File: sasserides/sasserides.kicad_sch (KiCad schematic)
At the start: 128 parts, among them J1 Conn_02x16_Odd_Even, Q1 2N7002

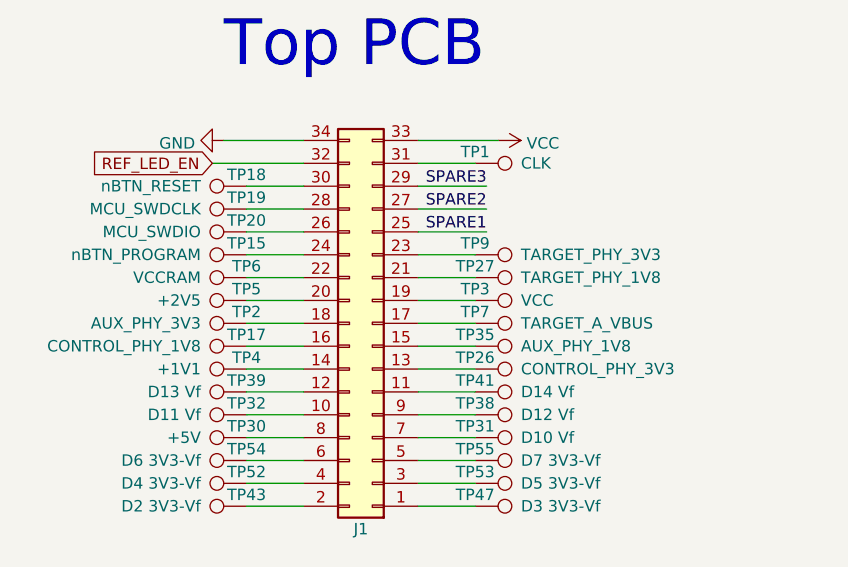
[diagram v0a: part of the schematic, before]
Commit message: Fix test points
	*Move TP7, TP9, & TP15 to correct locations
	*Swap TARGET_A_VBUS AND AUX_PHY_3V3 on MUX1
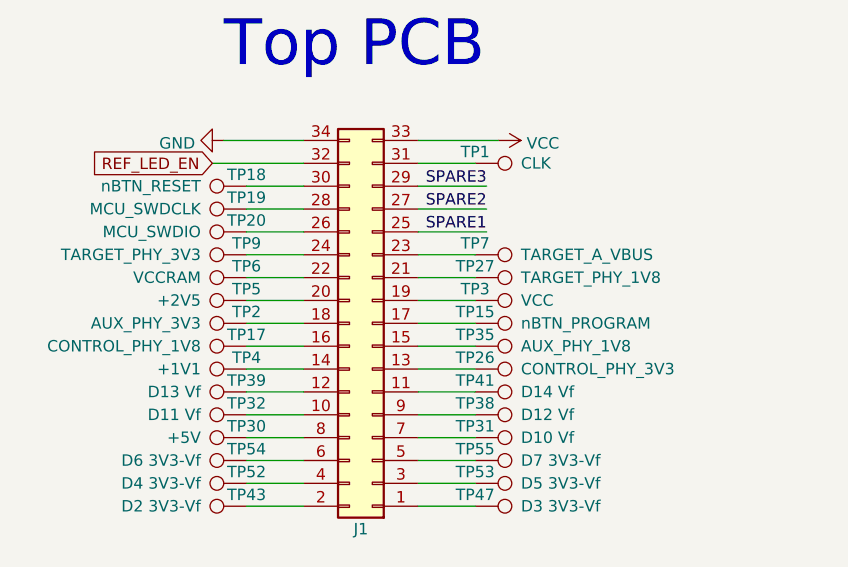
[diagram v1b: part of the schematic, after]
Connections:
- net at J1.17 (Pin_17): now also TP15.1; no longer TP7.1
- net at J1.23 (Pin_23): now also TP7.1; no longer TP9.1
- net at J1.24 (Pin_24): now also TP9.1; no longer TP15.1
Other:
- moved on the sheet: TP15, TP7, TP9
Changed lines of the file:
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@@
     )
   )
-  (symbol (lib_id "Connector:TestPoint") (at 91.44 72.39 270) (mirror x) (unit 1)
+  (symbol (lib_id "Connector:TestPoint") (at 91.44 64.77 270) (mirror x) (unit 1)
     (in_bom yes) (on_board yes) (dnp no)
-    (property "Reference" "TP7" (at 91.44 71.12 90)
+    (property "Reference" "TP7" (at 91.44 63.5 90)
       (effects (font (size 1.27 1.27)))
     )
-    (property "Value" "TARGET_A_VBUS" (at 96.52 72.39 90)
+    (property "Value" "TARGET_A_VBUS" (at 96.52 64.77 90)
       (effects (font (size 1.27 1.27)) (justify left))
     )
-    (property "Footprint" "tycho:HEADER-1x1-TESTPROBE" (at 91.44 67.31 0)
+    (property "Footprint" "tycho:HEADER-1x1-TESTPROBE" (at 91.44 59.69 0)
       (effects (font (size 1.27 1.27)) hide)
     )
-    (property "Datasheet" "~" (at 91.44 67.31 0)
+    (property "Datasheet" "~" (at 91.44 59.69 0)
       (effects (font (size 1.27 1.27)) hide)
     )
-    (property "Manufacturer" "Harwin Inc." (at 91.44 72.39 0)
+    (property "Manufacturer" "Harwin Inc." (at 91.44 64.77 0)
       (effects (font (size 1.27 1.27)) hide)
     )
-    (property "Part Number" "S25-512" (at 91.44 72.39 0)
+    (property "Part Number" "S25-512" (at 91.44 64.77 0)
       (effects (font (size 1.27 1.27)) hide)
     )
-    (property "Description" "SPRING PROBE SLEEVE" (at 91.44 72.39 0)
+    (property "Description" "SPRING PROBE SLEEVE" (at 91.44 64.77 0)
       (effects (font (size 1.27 1.27)) hide)
     )
@@
     )
   )
-  (symbol (lib_id "Connector:TestPoint") (at 91.44 64.77 270) (mirror x) (unit 1)
+  (symbol (lib_id "Connector:TestPoint") (at 66.04 64.77 90) (mirror x) (unit 1)
     (in_bom yes) (on_board yes) (dnp no)
-    (property "Reference" "TP9" (at 91.44 63.5 90)
+    (property "Reference" "TP9" (at 66.04 63.5 90)
       (effects (font (size 1.27 1.27)))
     )
-    (property "Value" "TARGET_PHY_3V3" (at 96.52 64.77 90)
+    (property "Value" "TARGET_PHY_3V3" (at 60.96 64.77 90)
       (effects (font (size 1.27 1.27)) (justify left))
     )
-    (property "Footprint" "tycho:HEADER-1x1-TESTPROBE" (at 91.44 59.69 0)
+    (property "Footprint" "tycho:HEADER-1x1-TESTPROBE" (at 66.04 69.85 0)
       (effects (font (size 1.27 1.27)) hide)
     )
-    (property "Datasheet" "~" (at 91.44 59.69 0)
+    (property "Datasheet" "~" (at 66.04 69.85 0)
       (effects (font (size 1.27 1.27)) hide)
     )
-    (property "Manufacturer" "Harwin Inc." (at 91.44 64.77 0)
+    (property "Manufacturer" "Harwin Inc." (at 66.04 64.77 0)
       (effects (font (size 1.27 1.27)) hide)
     )
-    (property "Part Number" "S25-512" (at 91.44 64.77 0)
+    (property "Part Number" "S25-512" (at 66.04 64.77 0)
       (effects (font (size 1.27 1.27)) hide)
     )
-    (property "Description" "SPRING PROBE SLEEVE" (at 91.44 64.77 0)
+    (property "Description" "SPRING PROBE SLEEVE" (at 66.04 64.77 0)
       (effects (font (size 1.27 1.27)) hide)
     )
@@
     )
   )
-  (symbol (lib_id "Connector:TestPoint") (at 66.04 64.77 90) (unit 1)
+  (symbol (lib_id "Connector:TestPoint") (at 91.44 72.39 270) (unit 1)
     (in_bom yes) (on_board yes) (dnp no)
-    (property "Reference" "TP15" (at 66.04 63.5 90)
+    (property "Reference" "TP15" (at 91.44 71.12 90)
       (effects (font (size 1.27 1.27)))
     )
-    (property "Value" "nBTN_PROGRAM" (at 60.96 64.77 90)
+    (property "Value" "nBTN_PROGRAM" (at 96.52 72.39 90)
       (effects (font (size 1.27 1.27)) (justify left))
     )
-    (property "Footprint" "tycho:HEADER-1x1-TESTPROBE" (at 66.04 59.69 0)
+    (property "Footprint" "tycho:HEADER-1x1-TESTPROBE" (at 91.44 77.47 0)
       (effects (font (size 1.27 1.27)) hide)
     )
-    (property "Datasheet" "~" (at 66.04 59.69 0)
+    (property "Datasheet" "~" (at 91.44 77.47 0)
       (effects (font (size 1.27 1.27)) hide)
     )
-    (property "Manufacturer" "Harwin Inc." (at 66.04 64.77 0)
+    (property "Manufacturer" "Harwin Inc." (at 91.44 72.39 0)
       (effects (font (size 1.27 1.27)) hide)
     )
-    (property "Part Number" "S25-512" (at 66.04 64.77 0)
+    (property "Part Number" "S25-512" (at 91.44 72.39 0)
       (effects (font (size 1.27 1.27)) hide)
     )
-    (property "Description" "SPRING PROBE SLEEVE" (at 66.04 64.77 0)
+    (property "Description" "SPRING PROBE SLEEVE" (at 91.44 72.39 0)
       (effects (font (size 1.27 1.27)) hide)
     )

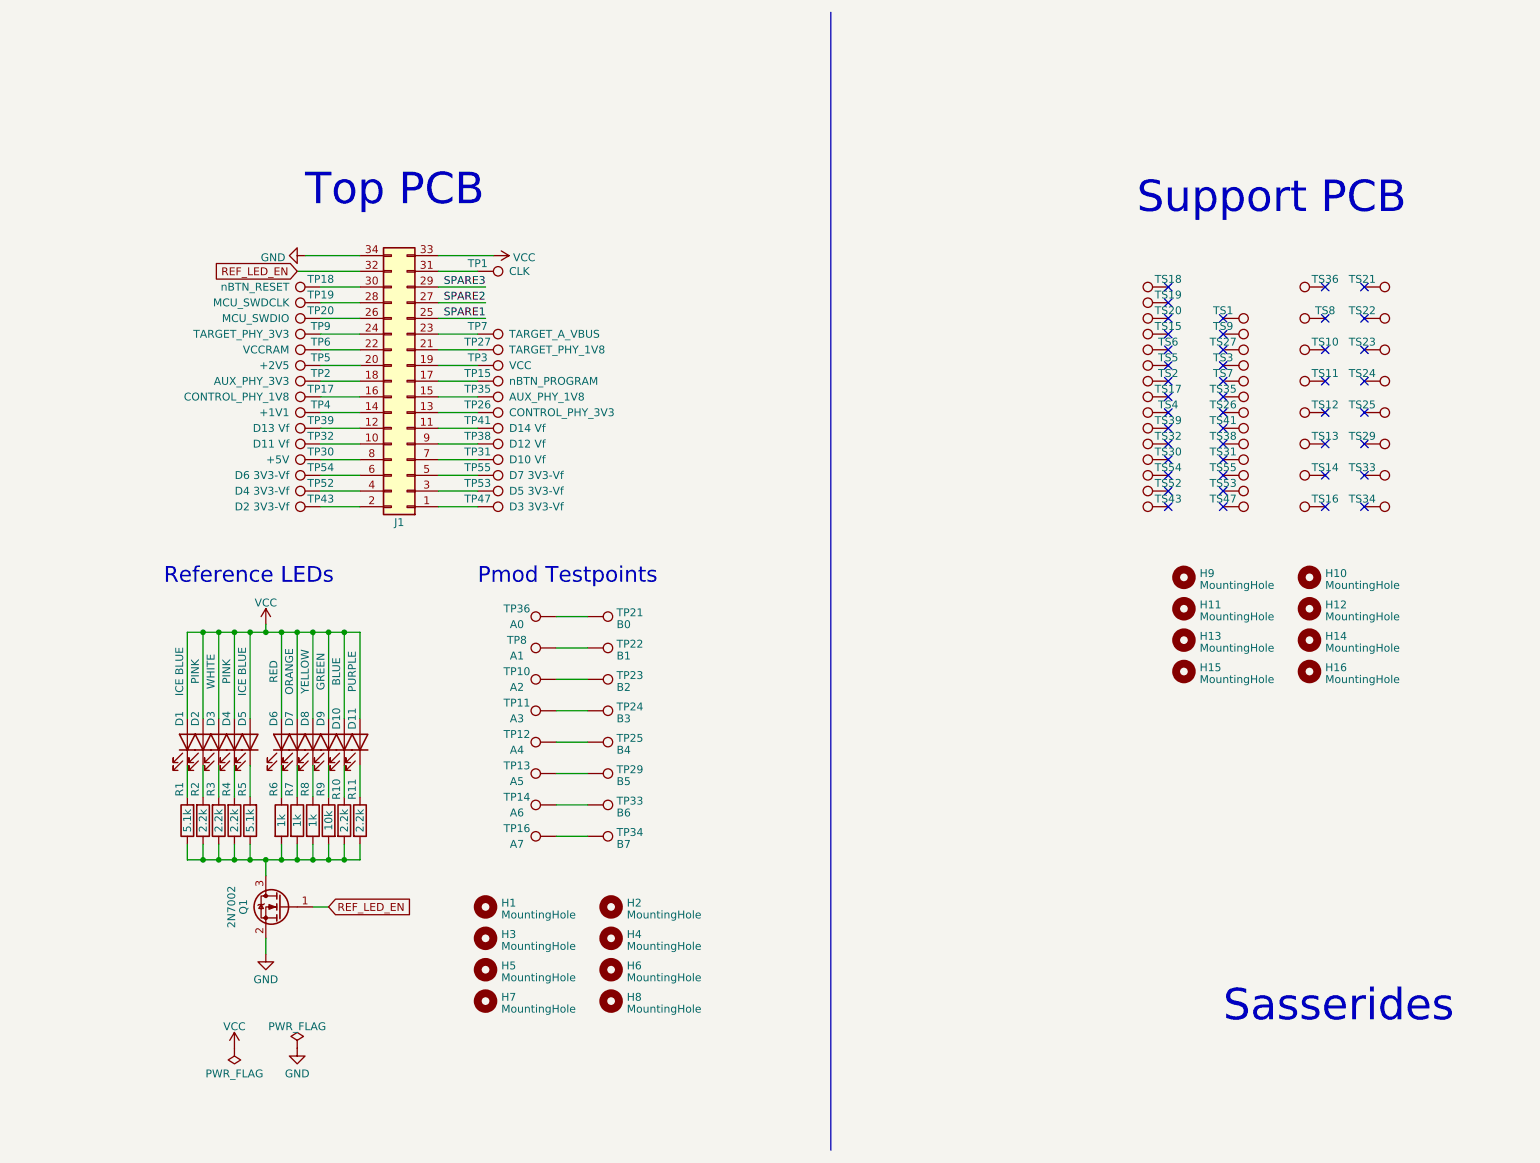
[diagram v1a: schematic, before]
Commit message: Rename Pmod TPs to A0-7/B0-7
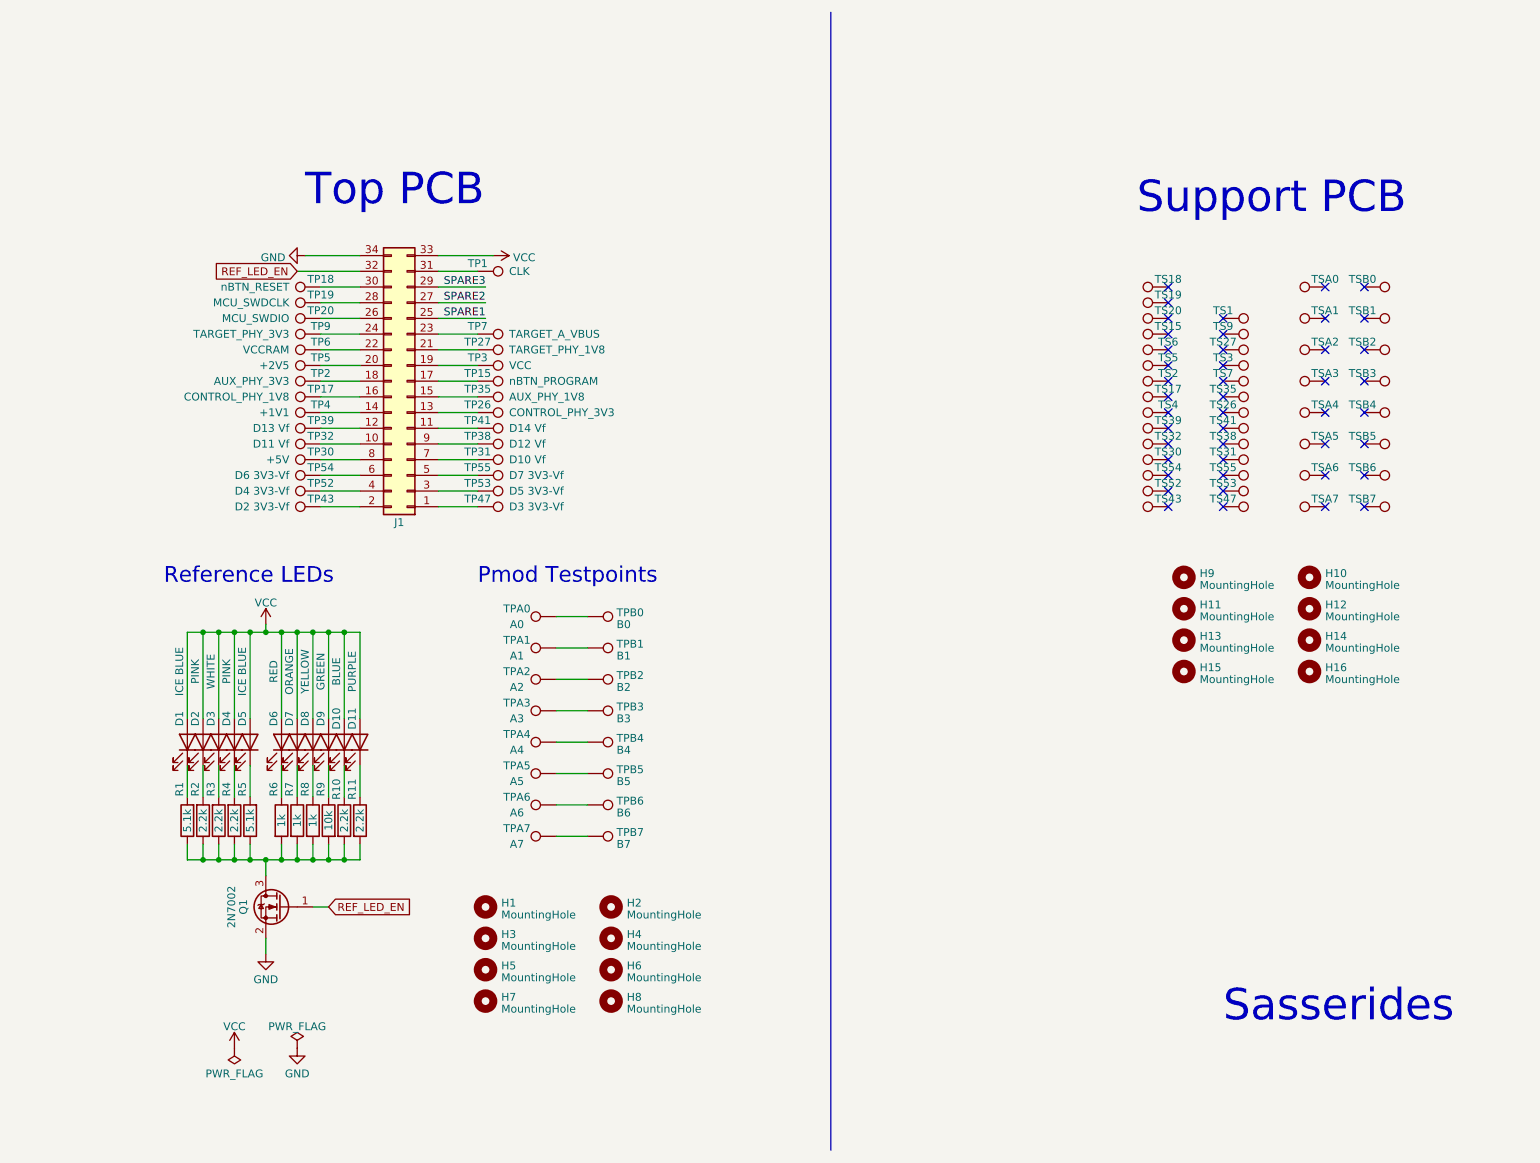
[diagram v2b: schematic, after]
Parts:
- renumbered TP36 to TPA0, TP8 to TPA1, TP10 to TPA2, TP11 to TPA3, TP12 to TPA4, TP13 to TPA5, TP14 to TPA6, TP16 to TPA7, TP21 to TPB0, TP22 to TPB1, TP23 to TPB2, TP24 to TPB3, TP25 to TPB4, TP29 to TPB5, TP33 to TPB6, TP34 to TPB7, TS36 to TSA0, TS8 to TSA1, TS10 to TSA2, TS11 to TSA3, TS12 to TSA4, TS13 to TSA5, TS14 to TSA6, TS16 to TSA7, TS21 to TSB0, TS22 to TSB1, TS23 to TSB2, TS24 to TSB3, TS25 to TSB4, TS29 to TSB5, TS33 to TSB6, TS34 to TSB7

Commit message: Clean up Sasserides silkscreen; Add meta data to all sheets
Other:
- company: (none) -> Copyright 2023 Great Scott Gadgets
- title: (none) -> Sasserides
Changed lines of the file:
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@@
 (kicad_sch (version 20230121) (generator eeschema)
   (paper "A4")
+  (title_block
+    (title "Sasserides")
+    (date "${DATE}")
+    (rev "${VERSION}")
+    (company "Copyright 2023 Great Scott Gadgets")
+    (comment 1 "Licensed under the CERN-OHL-P v2")
+  )
   (junction (at 49.53 113.03) (diameter 0) (color 0 0 0 0)
   )

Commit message: Change 34 pin header on Sasserides-A to shrouded type.
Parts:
- J1: footprint Connector_PinHeader_2.54mm:PinHeader_2x17_P2.54mm_Vertical -> tycho:shrouded_pin-header_2x17
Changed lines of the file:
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@@
       (effects (font (size 1.27 1.27)) hide)
     )
-    (property "Footprint" "Connector_PinHeader_2.54mm:PinHeader_2x17_P2.54mm_Vertical" (at 80.01 72.39 0)
+    (property "Footprint" "tycho:shrouded_pin-header_2x17" (at 80.01 72.39 0)
       (effects (font (size 1.27 1.27)) hide)
     )

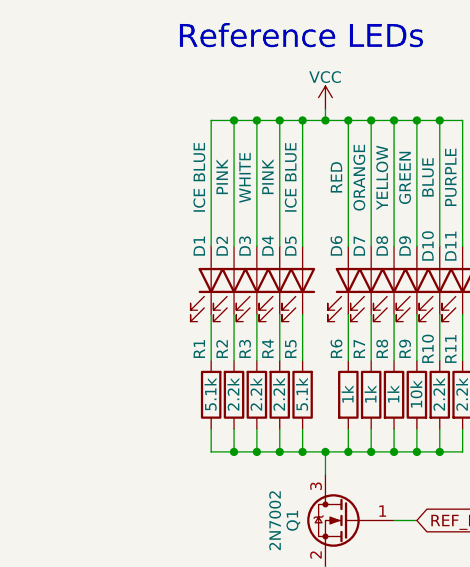
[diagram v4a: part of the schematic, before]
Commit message: Add 1uF VCC capacitor near LEDs.
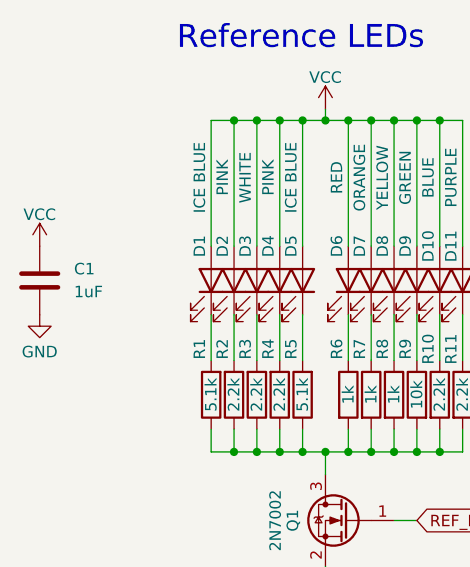
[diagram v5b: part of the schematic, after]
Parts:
- added C1: 1uF, Capacitor_SMD:C_0805_2012Metric, symbol Device:C
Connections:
- net GND: now also C1.2
- net VCC: now also C1.1
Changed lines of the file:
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@@
     )
   )
+  (symbol (lib_id "power:GND") (at 25.4 134.62 0) (unit 1)
+    (in_bom yes) (on_board yes) (dnp no) (fields_autoplaced)
+    (property "Reference" "#PWR08" (at 25.4 140.97 0)
+      (effects (font (size 1.27 1.27)) hide)
+    )
+    (property "Value" "GND" (at 25.4 138.7555 0)
+      (effects (font (size 1.27 1.27)))
+    )
+    (property "Footprint" "" (at 25.4 134.62 0)
+      (effects (font (size 1.27 1.27)) hide)
+    )
+    (property "Datasheet" "" (at 25.4 134.62 0)
+      (effects (font (size 1.27 1.27)) hide)
+    )
+    (pin "1")
+    (instances
+      (project "sasserides"
+        (path "/29d14f83-224e-4982-8820-b9fb63f3a50c"
+          (reference "#PWR08") (unit 1)
+        )
+      )
+    )
+  )
   (symbol (lib_id "Connector:TestPoint") (at 91.44 74.93 270) (mirror x) (unit 1)
     (in_bom yes) (on_board yes) (dnp no)
@@
     )
   )
+  (symbol (lib_id "power:VCC") (at 25.4 127 0) (unit 1)
+    (in_bom yes) (on_board yes) (dnp no)
+    (property "Reference" "#PWR07" (at 25.4 130.81 0)
+      (effects (font (size 1.27 1.27)) hide)
+    )
+    (property "Value" "VCC" (at 25.4 123.4981 0)
+      (effects (font (size 1.27 1.27)))
+    )
+    (property "Footprint" "" (at 25.4 127 0)
+      (effects (font (size 1.27 1.27)) hide)
+    )
+    (property "Datasheet" "" (at 25.4 127 0)
+      (effects (font (size 1.27 1.27)) hide)
+    )
+    (pin "1")
+    (instances
+      (project "sasserides"
+        (path "/29d14f83-224e-4982-8820-b9fb63f3a50c"
+          (reference "#PWR07") (unit 1)
+        )
+      )
+    )
+  )
   (symbol (lib_id "power:GND") (at 62.23 180.34 0) (unit 1)
     (in_bom yes) (on_board yes) (dnp no) (fields_autoplaced)
@@
         )
       )
+    )
+  )
+  (symbol (lib_id "Device:C") (at 25.4 130.81 0) (unit 1)
+    (in_bom yes) (on_board yes) (dnp no) (fields_autoplaced)
+    (property "Reference" "C1" (at 29.21 129.54 0)
+      (effects (font (size 1.27 1.27)) (justify left))
+    )
+    (property "Value" "1uF" (at 29.21 132.08 0)
+      (effects (font (size 1.27 1.27)) (justify left))
+    )
+    (property "Footprint" "Capacitor_SMD:C_0805_2012Metric" (at 26.3652 134.62 0)
+      (effects (font (size 1.27 1.27)) hide)
+    )
+    (property "Datasheet" "~" (at 25.4 130.81 0)
+      (effects (font (size 1.27 1.27)) hide)
+    )
+    (pin "1")
+    (pin "2")
+    (instances
+      (project "sasserides"
+        (path "/29d14f83-224e-4982-8820-b9fb63f3a50c"
+          (reference "C1") (unit 1)
+        )
+      )
